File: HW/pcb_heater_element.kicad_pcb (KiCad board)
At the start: 2 copper layers, 100 x 300 mm, 0 parts

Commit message: Progress
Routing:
- net (no net): vias 0 -> 8
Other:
- board size 100 x 300 mm -> 107.2 x 300 mm
- board text added: "- trace width 4 mm - unit length = 172 mm (2 lines + 2 arcs) - total units = 294 mm / 16 mm = 18.375 = 18 segments - total trace length per heater: 3096 mm - total trace length (x3 heaters) = 9.288 meters - At 20°C x3 heater have 1.24 Ohm resistance - At 20°C, for a 35°C rise, I need 5.7 A, resitance becomes 1.51 Ohm, 8.5 V drop - Power needed is 8.5 * 5.7 = 48.5 W - Using 12 V, to get the same p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"
- board text removed: "- trace width 4 mm - unit length = 172 mm (2 lines + 2 arcs) - total units = 294 mm / 16 mm = 18.375 = 18 segments - total trace length per heater: 3096 mm - total trace length (x3 heaters) = 9.288 meters - At 20°C x3 heater have 1.24 Ohm resistance - At 20°C, for a 35°C rise, I need 5.7A, resitance becomes 1.51 Ohm - Using 5V, that will be P = I*R = 28.5W needed"
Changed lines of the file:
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@@
     )
     (pad_to_mask_clearance 0)
-    (grid_origin 114.75 60)
+    (grid_origin 111.750732 214.5)
     (pcbplotparams
       (layerselection 0x00010fc_ffffffff)
@@
       (drillshape 0)
       (scaleselection 1)
-      (outputdirectory "gerbers/")
+      (outputdirectory "gerbers/heater/")
     )
   )
@@
   (gr_line (start 114.75 93.25) (end 208.75 93.25) (layer "Dwgs.User") (width 0.15))
   (gr_line (start 114.75 221.25) (end 208.75 221.25) (layer "Dwgs.User") (width 0.15))
-  (gr_rect (start 111.75 57) (end 211.75 357) (layer "Edge.Cuts") (width 0.1) (fill none))
+  (gr_line (start 111.75 223.84) (end 111.75 357) (layer "Edge.Cuts") (width 0.1))
+  (gr_line (start 211.75 214.5) (end 211.75 57) (layer "Edge.Cuts") (width 0.1))
+  (gr_line (start 211.75 357) (end 111.75 357) (layer "Edge.Cuts") (width 0.1))
+  (gr_line (start 111.75 57) (end 211.75 57) (layer "Edge.Cuts") (width 0.1))
+  (gr_arc (start 205.675 220.9) (mid 204.501525 219.288514) (end 205.6 217.625) (layer "Edge.Cuts") (width 0.1))
+  (gr_line (start 105.675732 220.9) (end 111.230732 223.27811) (layer "Edge.Cuts") (width 0.1))
+  (gr_arc (start 111.750732 214.5) (mid 111.657701 214.869137) (end 111.400732 215.15) (layer "Edge.Cuts") (width 0.1))
+  (gr_line (start 111.400732 215.15) (end 105.600732 217.625) (layer "Edge.Cuts") (width 0.1))
+  (gr_line (start 211.749268 223.84) (end 211.75 357) (layer "Edge.Cuts") (width 0.1))
+  (gr_line (start 111.750732 214.5) (end 111.75 57) (layer "Edge.Cuts") (width 0.1))
+  (gr_line (start 211.4 215.15) (end 205.6 217.625) (layer "Edge.Cuts") (width 0.1))
+  (gr_arc (start 105.675 220.9) (mid 104.501525 219.288514) (end 105.6 217.625) (layer "Edge.Cuts") (width 0.1))
+  (gr_arc (start 211.75 214.5) (mid 211.656969 214.869137) (end 211.4 215.15) (layer "Edge.Cuts") (width 0.1))
+  (gr_arc (start 211.23 223.27811) (mid 211.565616 223.488836) (end 211.749268 223.84) (layer "Edge.Cuts") (width 0.1))
+  (gr_line (start 205.675 220.9) (end 211.23 223.27811) (layer "Edge.Cuts") (width 0.1))
+  (gr_arc (start 111.230732 223.27811) (mid 111.566348 223.488836) (end 111.75 223.84) (layer "Edge.Cuts") (width 0.1))
   (gr_text "JLCJLCJLCJLC" (at 161.75 355.25) (layer "F.SilkS")
     (effects (font (size 1 1) (thickness 0.25)))
   )
-  (gr_text "- trace width 4 mm\n- unit length = 172 mm (2 lines + 2 arcs)\n- total units = 294 mm / 16 mm = 18.375 = 18 segments\n- total trace length per heater: 3096 mm\n- total trace length (x3 heaters) = 9.288 meters\n\n- At 20°C x3 heater have 1.24 Ohm resistance\n- At 20°C, for a 35°C rise, I need 5.7A, resitance becomes 1.51 Ohm\n- Using 5V, that will be P = I*R = 28.5W needed" (at 230.75 94) (layer "Cmts.User")
+  (gr_text "- trace width 4 mm\n- unit length = 172 mm (2 lines + 2 arcs)\n- total units = 294 mm / 16 mm = 18.375 = 18 segments\n- total trace length per heater: 3096 mm\n- total trace length (x3 heaters) = 9.288 meters\n\n- At 20°C x3 heater have 1.24 Ohm resistance\n- At 20°C, for a 35°C rise, I need 5.7 A, resitance becomes 1.51 Ohm, 8.5 V drop\n- Power needed is 8.5 * 5.7 = 48.5 W\n- Using 12 V, to get the same power draw I need only 2 A, regulated by NMOS\n" (at 230.75 94) (layer "Cmts.User")
     (effects (font (size 5 5) (thickness 0.05)) (justify left))
   )
@@
   (segment (start 120.75 167.25) (end 202.75 167.25) (width 4) (layer "F.Cu") (net 0))
   (segment (start 202.75 287.25) (end 120.75 287.25) (width 4) (layer "F.Cu") (net 0))
+  (via (at 111.750732 218.75) (size 0.8) (drill 0.4) (layers "F.Cu" "B.Cu") (free) (net 0))
+  (via (at 111.750732 220.75) (size 0.8) (drill 0.4) (layers "F.Cu" "B.Cu") (free) (net 0))
+  (via (at 111.750732 217.75) (size 0.8) (drill 0.4) (layers "F.Cu" "B.Cu") (free) (net 0))
+  (via (at 111.750732 221.75) (size 0.8) (drill 0.4) (layers "F.Cu" "B.Cu") (free) (net 0))
+  (via (at 111.750732 216.75) (size 0.8) (drill 0.4) (layers "F.Cu" "B.Cu") (free) (net 0))
+  (via (at 111.750732 215.75) (size 0.8) (drill 0.4) (layers "F.Cu" "B.Cu") (free) (net 0))
+  (via (at 111.750732 219.75) (size 0.8) (drill 0.4) (layers "F.Cu" "B.Cu") (free) (net 0))
+  (via (at 111.750732 222.75) (size 0.8) (drill 0.4) (layers "F.Cu" "B.Cu") (free) (net 0))
   (zone (net 0) (net_name "") (layer "F.Cu") (hatch edge 0.508)
     (connect_pads (clearance 0))
@@
       )
     )
+  )
+  (zone (net 0) (net_name "") (layer "F.Mask") (hatch edge 0.508)
+    (connect_pads (clearance 0))
+    (min_thickness 0.254) (filled_areas_thickness no)
+    (fill yes (thermal_gap 0.508) (thermal_bridge_width 0.508))
+    (polygon
+      (pts
+        (xy 167.75 209.25)
+        (xy 156.75 209.25)
+        (xy 156.75 205.25)
+        (xy 167.75 205.25)
+      )
+    )

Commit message: Sectioned schematic, reqorked heater trace length and thickness
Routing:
- net (no net): track 3034.0 -> 4416.0 mm, vias 8 -> 0
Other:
- outline, holes or cut-outs redrawn
- board text added: "- trace width 2 mm - unit length = (2 lines + 2 arcs) = 82 * 2 + 8.6 * 2 = 181.2 mm - total units = 26 - total trace length per heater: 4.88 m - total trace length (x3 heaters) = 14.6 meters"
- board text removed: "- trace width 4 mm - unit length = 172 mm (2 lines + 2 arcs) - total units = 294 mm / 16 mm = 18.375 = 18 segments - total trace length per heater: 3096 mm - total trace length (x3 heaters) = 9.288 meters - At 20°C x3 heater have 1.24 Ohm resistance - At 20°C, for a 35°C rise, I need 5.7 A, resitance becomes 1.51 Ohm, 8.5 V drop - Power needed is 8.5 * 5.7 = 48.5 W - Using 12 V, to get the same p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"

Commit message: Fixed board, big work in schematic, to finish
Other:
- outline, holes or cut-outs redrawn
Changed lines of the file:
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@@
     )
     (pad_to_mask_clearance 0)
-    (grid_origin 111.75 357)
+    (grid_origin 211.75 57)
     (pcbplotparams
       (layerselection 0x00010fc_ffffffff)
@@
   (gr_rect (start 114.75 60) (end 208.75 354.5) (layer "Dwgs.User") (width 0.15) (fill none))
   (gr_rect (start 208.75 349) (end 202.75 355) (layer "Dwgs.User") (width 0.15) (fill none))
-  (gr_line (start 111.75 223.84) (end 111.75 357) (layer "Edge.Cuts") (width 0.1))
-  (gr_line (start 211.75 214.5) (end 211.75 57) (layer "Edge.Cuts") (width 0.1))
-  (gr_line (start 211.75 357) (end 111.75 357) (layer "Edge.Cuts") (width 0.1))
-  (gr_line (start 111.75 57) (end 211.75 57) (layer "Edge.Cuts") (width 0.1))
+  (gr_arc (start 111.157701 216.269136) (mid 111.6577 215.769137) (end 112.157698 216.269136) (layer "Edge.Cuts") (width 0.1))
+  (gr_line (start 111.75 223.84) (end 111.75 355.5) (layer "Edge.Cuts") (width 0.1))
+  (gr_line (start 211.75 214.5) (end 211.75 58.5) (layer "Edge.Cuts") (width 0.1))
+  (gr_line (start 210.25 357) (end 113.25 357) (layer "Edge.Cuts") (width 0.1))
+  (gr_line (start 112.1577 222.269138) (end 112.157698 216.269136) (layer "Edge.Cuts") (width 0.1))
+  (gr_line (start 113.25 57) (end 210.25 57) (layer "Edge.Cuts") (width 0.1))
   (gr_arc (start 205.675 220.9) (mid 204.501525 219.288514) (end 205.6 217.625) (layer "Edge.Cuts") (width 0.1))
   (gr_line (start 105.75 220.9) (end 111.230732 223.27811) (layer "Edge.Cuts") (width 0.1))
+  (gr_arc (start 113.25 357) (mid 112.18934 356.56066) (end 111.75 355.5) (layer "Edge.Cuts") (width 0.1))
   (gr_arc (start 111.750732 214.5) (mid 111.657701 214.869137) (end 111.400732 215.15) (layer "Edge.Cuts") (width 0.1))
+  (gr_arc (start 112.1577 222.269138) (mid 111.657701 222.769137) (end 111.157702 222.269138) (layer "Edge.Cuts") (width 0.1))
+  (gr_line (start 111.157701 216.269136) (end 111.157702 222.269138) (layer "Edge.Cuts") (width 0.1))
   (gr_line (start 111.400732 215.15) (end 105.675 217.625) (layer "Edge.Cuts") (width 0.1))
-  (gr_line (start 211.749268 223.84) (end 211.75 357) (layer "Edge.Cuts") (width 0.1))
-  (gr_line (start 111.750732 214.5) (end 111.75 57) (layer "Edge.Cuts") (width 0.1))
+  (gr_arc (start 210.25 57) (mid 211.31066 57.43934) (end 211.75 58.5) (layer "Edge.Cuts") (width 0.1))
+  (gr_line (start 211.749268 223.84) (end 211.75 355.5) (layer "Edge.Cuts") (width 0.1))
+  (gr_line (start 111.750732 214.5) (end 111.75 58.5) (layer "Edge.Cuts") (width 0.1))
+  (gr_arc (start 211.75 355.5) (mid 211.31066 356.56066) (end 210.25 357) (layer "Edge.Cuts") (width 0.1))
   (gr_line (start 211.4 215.15) (end 205.6 217.625) (layer "Edge.Cuts") (width 0.1))
   (gr_arc (start 105.75 220.9) (mid 104.576521 219.288528) (end 105.675 217.625) (layer "Edge.Cuts") (width 0.1))
@@
   (gr_line (start 205.675 220.9) (end 211.23 223.27811) (layer "Edge.Cuts") (width 0.1))
   (gr_arc (start 111.230732 223.27811) (mid 111.566348 223.488836) (end 111.75 223.84) (layer "Edge.Cuts") (width 0.1))
+  (gr_arc (start 111.75 58.5) (mid 112.18934 57.43934) (end 113.25 57) (layer "Edge.Cuts") (width 0.1))
   (gr_text "JLCJLCJLCJLC" (at 161.75 355.25) (layer "F.SilkS")
     (effects (font (size 1 1) (thickness 0.25)))

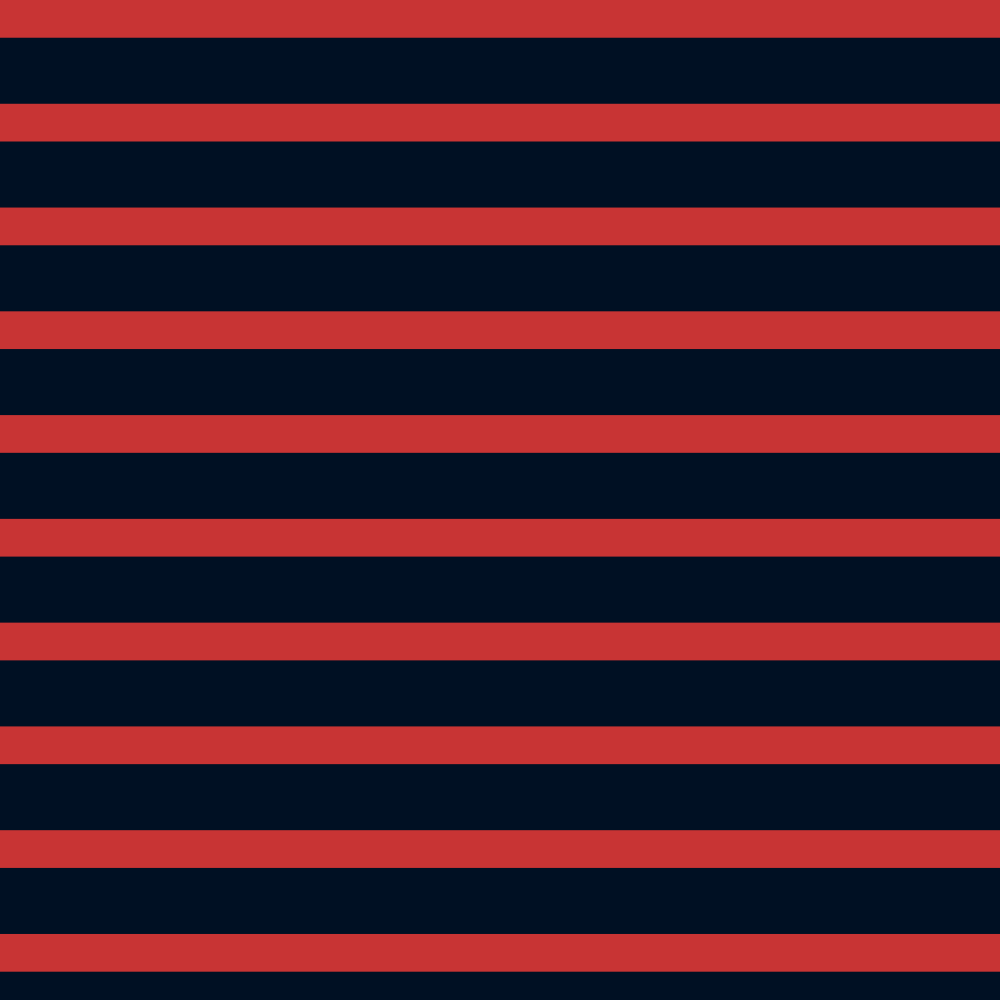
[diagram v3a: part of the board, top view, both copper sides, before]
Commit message: Finished sch, to be checked. Initial components layout
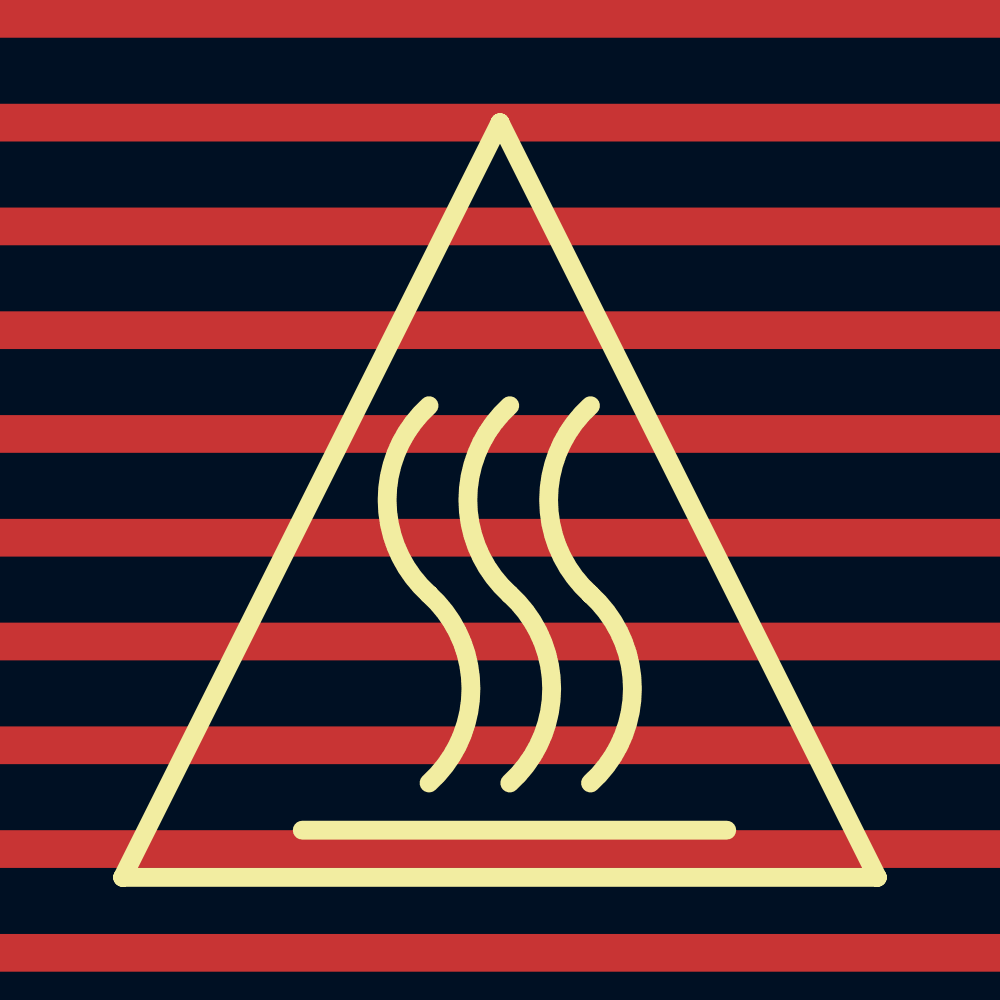
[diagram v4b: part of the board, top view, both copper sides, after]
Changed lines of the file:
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@@
   (gr_line (start 201.75 347.95) (end 210.75 347.95) (layer "F.SilkS") (width 0.2))
   (gr_line (start 121.75 57.95) (end 121.75 66.05) (layer "F.SilkS") (width 0.2))
+  (gr_arc (start 166.25 201.5) (mid 164.029083 196.5) (end 166.25 191.5) (layer "F.SilkS") (width 1))
   (gr_line (start 112.75 57.95) (end 121.75 57.95) (layer "F.SilkS") (width 0.2))
   (gr_line (start 201.75 66.05) (end 201.75 57.95) (layer "F.SilkS") (width 0.2))
+  (gr_arc (start 166.25 201.5) (mid 168.470917 206.5) (end 166.25 211.5) (layer "F.SilkS") (width 1))
   (gr_line (start 210.75 66.05) (end 201.75 66.05) (layer "F.SilkS") (width 0.2))
   (gr_line (start 210.75 356.05) (end 201.75 356.05) (layer "F.SilkS") (width 0.2))
+  (gr_line (start 141.45307 216.5) (end 181.45307 216.5) (layer "F.SilkS") (width 1))
+  (gr_line (start 141.45307 216.5) (end 161.45307 176.5) (layer "F.SilkS") (width 1))
+  (gr_arc (start 157.691834 201.5) (mid 159.912751 206.5) (end 157.691834 211.5) (layer "F.SilkS") (width 1))
+  (gr_arc (start 161.970917 201.5) (mid 164.191834 206.5) (end 161.970917 211.5) (layer "F.SilkS") (width 1))
   (gr_line (start 121.75 347.950001) (end 121.75 356.050001) (layer "F.SilkS") (width 0.2))
   (gr_line (start 201.75 57.95) (end 210.75 57.95) (layer "F.SilkS") (width 0.2))
   (gr_line (start 121.75 66.05) (end 112.75 66.05) (layer "F.SilkS") (width 0.2))
+  (gr_line (start 181.45307 216.5) (end 161.45307 176.5) (layer "F.SilkS") (width 1))
+  (gr_line (start 150.970917 214) (end 173.470917 214) (layer "F.SilkS") (width 1))
+  (gr_arc (start 161.970917 201.5) (mid 159.75 196.5) (end 161.970917 191.5) (layer "F.SilkS") (width 1))
   (gr_line (start 112.75 347.950001) (end 121.75 347.950001) (layer "F.SilkS") (width 0.2))
+  (gr_arc (start 157.691834 201.5) (mid 155.470917 196.5) (end 157.691834 191.5) (layer "F.SilkS") (width 1))
   (gr_line (start 201.75 356.05) (end 201.75 347.95) (layer "F.SilkS") (width 0.2))
   (gr_line (start 114.75 159) (end 208.75 159) (layer "Dwgs.User") (width 0.15))
@@
   )
   (zone (net 0) (net_name "") (layer "F.Cu") (hatch edge 0.508)
-    (connect_pads (clearance 0))
+    (connect_pads no (clearance 0))
     (min_thickness 0.254) (filled_areas_thickness no)
     (fill yes (thermal_gap 0.508) (thermal_bridge_width 0.508))
@@
     )
   )
+  (group "" (id 442046a6-c938-43b3-b010-c9f508c58c80)
+    (members
+      3407777c-d948-490d-a2f0-b3ad3390e217
+      6995d692-6799-4a4b-8ee5-526e62999268
+    )
+  )
+  (group "" (id 454079b5-5f56-4005-9bb0-cb1842e256b8)
+    (members
+      9671bd96-bff1-43f9-b9b6-fdc331638949
+      ed15d2ab-884d-4309-8fc5-a20c99e91302
+    )
+  )
   (group "" (id 4c1d2d5d-5505-4737-9057-bc029fe30702)
     (members
@@
     )
   )
+  (group "" (id 67672e82-97e4-47ab-b957-cf9ca30dd2f4)
+    (members
+      9cb35d60-e2a6-4cef-b26f-35c25d9959a4
+      ec2952dd-055b-4f00-906e-4bdb54383563
+    )
+  )
   (group "" (id 857e11d7-714c-4fcc-a2a1-e882c8b84df0)
     (members
@@
     )
   )
+  (group "" (id 9b82df83-6901-4f7e-8da8-6aef52a68497)
+    (members
+      442046a6-c938-43b3-b010-c9f508c58c80
+      454079b5-5f56-4005-9bb0-cb1842e256b8
+      67672e82-97e4-47ab-b957-cf9ca30dd2f4
+      e8474e69-37bb-44f9-9316-d1494d8a4bbd
+    )
+  )
   (group "" (id a1e9a31a-6710-47f6-af90-b38d6e41977f)
     (members
@@
     )
   )
+  (group "" (id a82ed511-da4c-4b63-9d60-585267c54cae)
+    (members
+      91d57969-812a-41f8-a9ad-7a349eecedf0
+      94411f6d-f423-47ca-8c80-4f3cf0a79a62
+      9b82df83-6901-4f7e-8da8-6aef52a68497
+      db6a4193-7b6b-45ca-a1bc-47905534da96
+    )
+  )

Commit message: Sch finalized, added EMC stuff, user buttons and oled
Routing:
- net (no net): track 4416.0 -> 2177.5 mm
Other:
- board text added: "- trace width 2 mm - unit length = (2 lines + 2 arcs) = 81 * 2 + 17.78 * 2 = 197.5 mm - total units = 13 - total trace length per heater: 2.56 m - total trace length (x3 heaters) = 7.7 m"
- board text removed: "- trace width 2 mm - unit length = (2 lines + 2 arcs) = 82 * 2 + 8.6 * 2 = 181.2 mm - total units = 26 - total trace length per heater: 4.88 m - total trace length (x3 heaters) = 14.6 meters"

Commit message: Fix board, QOL fixes
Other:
- board size 107.2 x 300 mm -> 130.2 x 300 mm
- board text added: "- trace width 1.5 mm - unit length = (2 lines + 2 arcs) = 81 * 2 + 17.27875 * 2 = 196.6 mm - total full units = 12 - first unit is 83.5 + 81 + (17.27875*2) = 199 mm - last unit is 83 mm - total trace length per heater: 2.64 m - total trace length (x3 heaters) ~= 7.9 m"
- board text added: "JLCJLCJLC"
- board text removed: "- trace width 2 mm - unit length = (2 lines + 2 arcs) = 81 * 2 + 17.78 * 2 = 197.5 mm - total units = 13 - total trace length per heater: 2.56 m - total trace length (x3 heaters) = 7.7 m"
